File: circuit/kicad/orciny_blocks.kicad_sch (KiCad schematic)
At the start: 0 parts

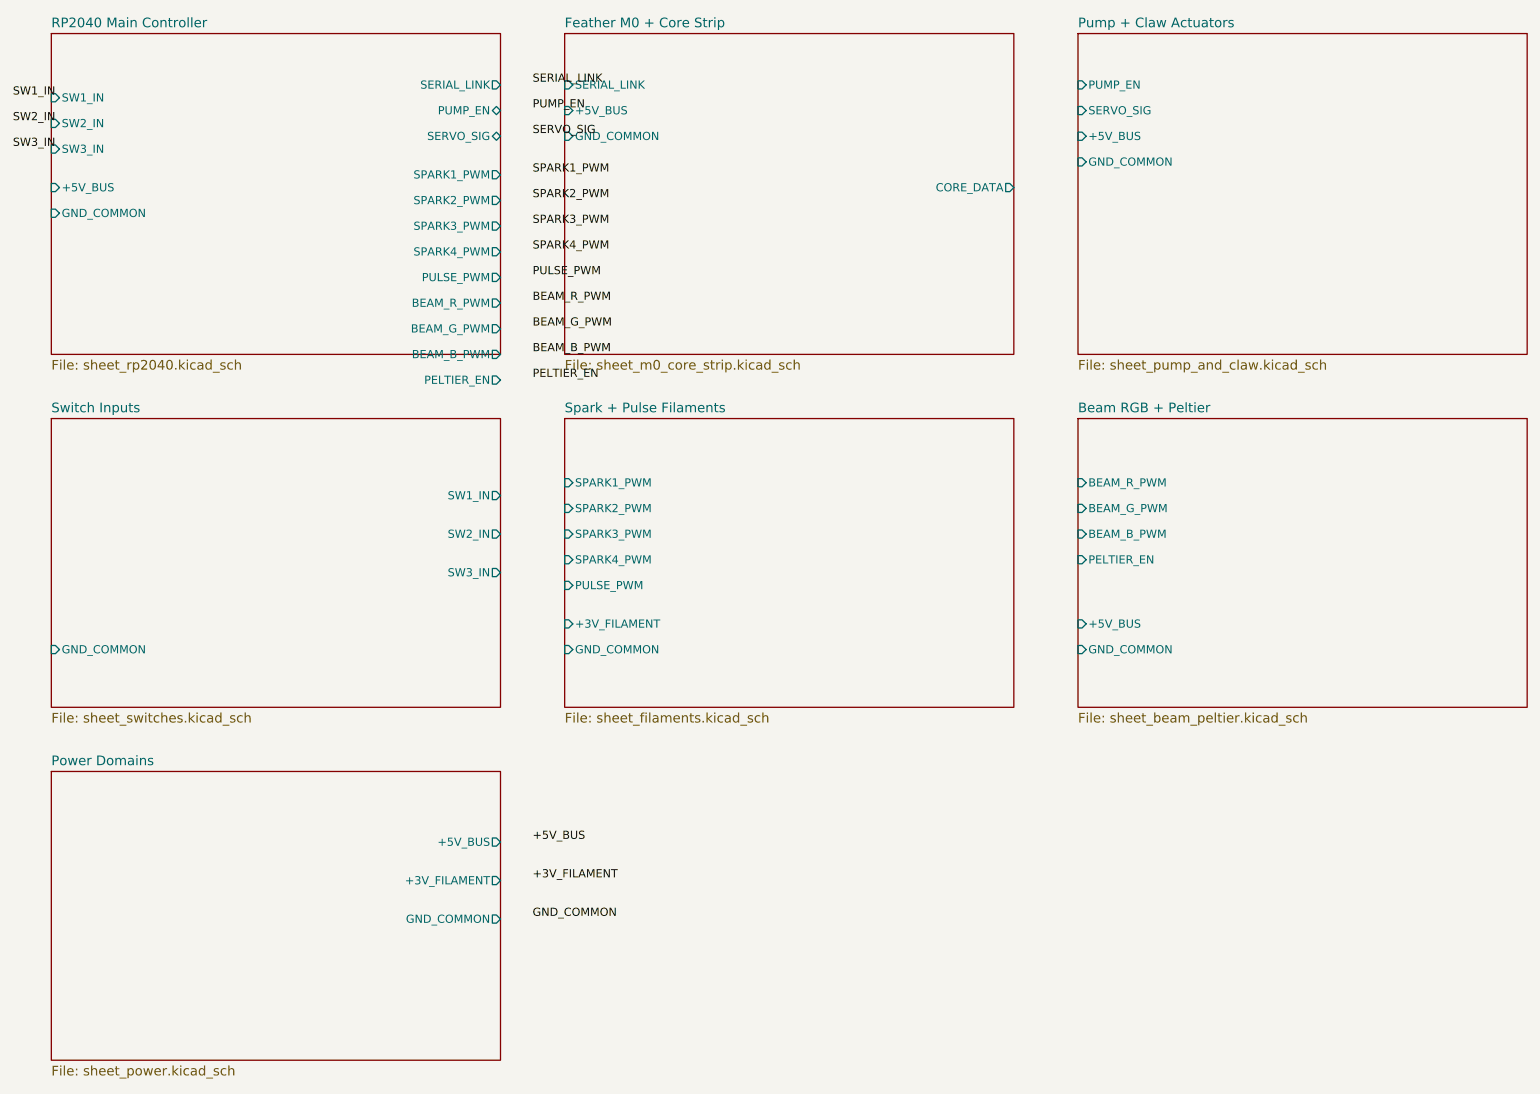
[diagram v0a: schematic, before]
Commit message: Merge Box updates, normalize circuit layout, and add Box sync workflow
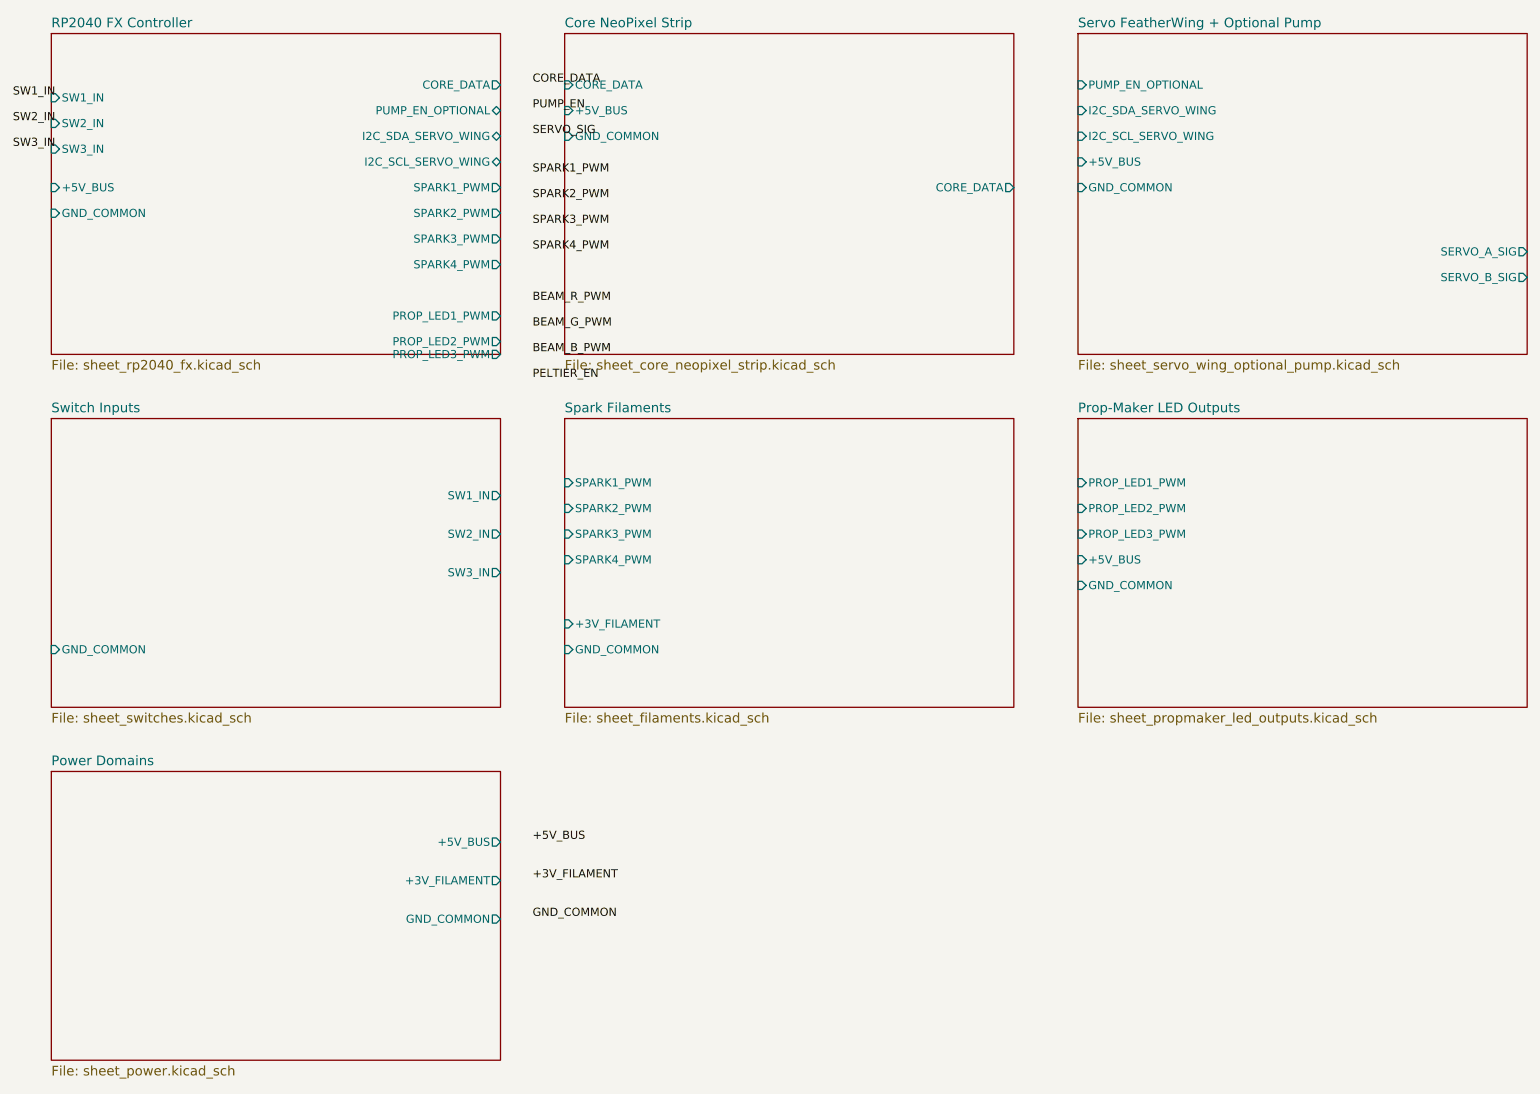
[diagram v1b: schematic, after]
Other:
- sheet Beam RGB + Peltier renamed Prop-Maker LED Outputs
- sheet Feather M0 + Core Strip renamed Core NeoPixel Strip
- sheet Pump + Claw Actuators renamed Servo FeatherWing + Optional Pump
- sheet RP2040 Main Controller renamed RP2040 FX Controller
- sheet Spark + Pulse Filaments renamed Spark Filaments
- sheet Core NeoPixel Strip: file sheet_m0_core_strip.kicad_sch -> sheet_core_neopixel_strip.kicad_sch
- sheet Core NeoPixel Strip ports: added none; removed SERIAL_LINK
- sheet Prop-Maker LED Outputs: file sheet_beam_peltier.kicad_sch -> sheet_propmaker_led_outputs.kicad_sch
- sheet Prop-Maker LED Outputs ports: added PROP_LED1_PWM, PROP_LED2_PWM, PROP_LED3_PWM; removed BEAM_B_PWM, BEAM_G_PWM, BEAM_R_PWM, PELTIER_EN
- sheet RP2040 FX Controller: file sheet_rp2040.kicad_sch -> sheet_rp2040_fx.kicad_sch
- sheet RP2040 FX Controller ports: added CORE_DATA, I2C_SCL_SERVO_WING, I2C_SDA_SERVO_WING, PROP_LED1_PWM, PROP_LED2_PWM, PROP_LED3_PWM, PUMP_EN_OPTIONAL; removed BEAM_B_PWM, BEAM_G_PWM, BEAM_R_PWM, PELTIER_EN, PULSE_PWM, PUMP_EN, SERIAL_LINK, SERVO_SIG
- sheet Servo FeatherWing + Optional Pump: file sheet_pump_and_claw.kicad_sch -> sheet_servo_wing_optional_pump.kicad_sch
- sheet Servo FeatherWing + Optional Pump ports: added I2C_SCL_SERVO_WING, I2C_SDA_SERVO_WING, PUMP_EN_OPTIONAL, SERVO_A_SIG, SERVO_B_SIG; removed PUMP_EN, SERVO_SIG
- sheet Spark Filaments ports: added none; removed PULSE_PWM
